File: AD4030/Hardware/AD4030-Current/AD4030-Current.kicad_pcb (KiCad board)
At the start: 2 copper layers, 0 parts

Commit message: Hardware
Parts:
- added C301: 0.1u, Capacitor_SMD:C_0603_1608Metric_Pad1.08x0.95mm_HandSolder, F.Cu at (-9.39, 62.3)
- added C302: 0.1u, Capacitor_SMD:C_0402_1005Metric_Pad0.74x0.62mm_HandSolder, B.Cu at (171.1, 102.2)
- added C303: 0.1u, Capacitor_SMD:C_0402_1005Metric_Pad0.74x0.62mm_HandSolder, B.Cu at (171.1, 103.3)
- added C304: 0.1u, Capacitor_SMD:C_0402_1005Metric_Pad0.74x0.62mm_HandSolder, B.Cu at (175.3, 93.6)
- added C305: 0.1u, Capacitor_SMD:C_0402_1005Metric_Pad0.74x0.62mm_HandSolder, B.Cu at (175.3, 94.6)
- added C306: 0.1u, Capacitor_SMD:C_0402_1005Metric_Pad0.74x0.62mm_HandSolder, B.Cu at (172.5, 93.6)
- added C307: 560p, Capacitor_SMD:C_0402_1005Metric_Pad0.74x0.62mm_HandSolder, F.Cu at (165.5, 99.0)
- added C308: 560p, Capacitor_SMD:C_0402_1005Metric_Pad0.74x0.62mm_HandSolder, F.Cu at (165.5, 94.3)
- added C309: 0.1u, Capacitor_SMD:C_0402_1005Metric_Pad0.74x0.62mm_HandSolder, B.Cu at (172.5, 94.6)
- added C310: 270p, Capacitor_SMD:C_0402_1005Metric_Pad0.74x0.62mm_HandSolder, F.Cu at (167.3, 96.6)
- added C311: 1u, Capacitor_SMD:C_0603_1608Metric_Pad1.08x0.95mm_HandSolder, B.Cu at (169.8, 90.9)
- added C312: 0.1u, Capacitor_SMD:C_0603_1608Metric_Pad1.08x0.95mm_HandSolder, F.Cu at (-9.39, 67.3)
- added C313: 0.1u, Capacitor_SMD:C_0603_1608Metric_Pad1.08x0.95mm_HandSolder, F.Cu at (-9.39, 69.8)
- added C314: 2u2/25V, Capacitor_SMD:C_0805_2012Metric_Pad1.18x1.45mm_HandSolder, B.Cu at (152.5, 82.2)
- added C315: 10u, Capacitor_SMD:C_0805_2012Metric_Pad1.18x1.45mm_HandSolder, B.Cu at (152.5, 86.4)
- added C316: 1u, Capacitor_SMD:C_0603_1608Metric_Pad1.08x0.95mm_HandSolder, F.Cu at (176.3, 90.9)
- added C317: 2n7, Capacitor_SMD:C_0603_1608Metric_Pad1.08x0.95mm_HandSolder, B.Cu at (173.9, 90.9)
- added C318: 10u, Capacitor_SMD:C_0805_2012Metric_Pad1.18x1.45mm_HandSolder, B.Cu at (152.5, 84.2)
- added C319: 10u, Capacitor_SMD:C_0805_2012Metric_Pad1.18x1.45mm_HandSolder, F.Cu at (163.2, 90.9)
- added C320: 0.1u, Capacitor_SMD:C_0603_1608Metric_Pad1.08x0.95mm_HandSolder, F.Cu at (-41.0, 49.7)
- added C321: 1u, Capacitor_SMD:C_0603_1608Metric_Pad1.08x0.95mm_HandSolder, F.Cu at (-41.0, 52.2)
- added C322: 0.1u, Capacitor_SMD:C_0603_1608Metric_Pad1.08x0.95mm_HandSolder, F.Cu at (-41.0, 54.7)
- added C323: 1u, Capacitor_SMD:C_0603_1608Metric_Pad1.08x0.95mm_HandSolder, F.Cu at (-41.0, 57.2)
- added C401: 0.1u, Capacitor_SMD:C_0603_1608Metric_Pad1.08x0.95mm_HandSolder, F.Cu at (-36.7, 49.7)
- added C402: 1u, Capacitor_SMD:C_0603_1608Metric_Pad1.08x0.95mm_HandSolder, F.Cu at (-36.7, 52.2)
- added C403: 0.1u, Capacitor_SMD:C_0603_1608Metric_Pad1.08x0.95mm_HandSolder, F.Cu at (-36.7, 54.7)
- added C404: 1u, Capacitor_SMD:C_0603_1608Metric_Pad1.08x0.95mm_HandSolder, F.Cu at (-36.7, 57.2)
- added C405: 0.1u, Capacitor_SMD:C_0603_1608Metric_Pad1.08x0.95mm_HandSolder, F.Cu at (-32.3, 49.7)
- added C406: 1u, Capacitor_SMD:C_0603_1608Metric_Pad1.08x0.95mm_HandSolder, F.Cu at (-32.3, 52.2)
- added C407: 0.1u, Capacitor_SMD:C_0603_1608Metric_Pad1.08x0.95mm_HandSolder, F.Cu at (-32.3, 54.7)
- added C408: 1u, Capacitor_SMD:C_0603_1608Metric_Pad1.08x0.95mm_HandSolder, F.Cu at (-32.3, 57.2)
- added C409: C, Capacitor_SMD:C_0603_1608Metric_Pad1.08x0.95mm_HandSolder, F.Cu at (124.3, 99.8)
- added C410: C, Capacitor_SMD:C_0603_1608Metric_Pad1.08x0.95mm_HandSolder, F.Cu at (136.0, 99.8)
- added C411: C, Capacitor_SMD:C_0603_1608Metric_Pad1.08x0.95mm_HandSolder, F.Cu at (147.7, 99.8)
- added C412: 0.1u, Capacitor_SMD:C_0603_1608Metric_Pad1.08x0.95mm_HandSolder, B.Cu at (113.0, 97.6)
- added C413: 0.1u, Capacitor_SMD:C_0603_1608Metric_Pad1.08x0.95mm_HandSolder, B.Cu at (121.1, 97.6)
- added C414: 0.1u, Capacitor_SMD:C_0603_1608Metric_Pad1.08x0.95mm_HandSolder, B.Cu at (132.8, 97.6)
- added C415: 0.1u, Capacitor_SMD:C_0603_1608Metric_Pad1.08x0.95mm_HandSolder, B.Cu at (144.5, 97.6)
- added C416: 0.1u, Capacitor_SMD:C_0603_1608Metric_Pad1.08x0.95mm_HandSolder, B.Cu at (120.8, 104.0)
- added C417: 0.1u, Capacitor_SMD:C_0603_1608Metric_Pad1.08x0.95mm_HandSolder, F.Cu at (-0.29, 38.1)
- added C418: 0.1u, Capacitor_SMD:C_0603_1608Metric_Pad1.08x0.95mm_HandSolder, F.Cu at (4.06, 18.0)
- added C419: 0.1u, Capacitor_SMD:C_0603_1608Metric_Pad1.08x0.95mm_HandSolder, B.Cu at (108.1, 97.6)
- added C420: 0.1u, Capacitor_SMD:C_0603_1608Metric_Pad1.08x0.95mm_HandSolder, B.Cu at (116.1, 97.6)
- added C421: 0.1u, Capacitor_SMD:C_0603_1608Metric_Pad1.08x0.95mm_HandSolder, B.Cu at (127.7, 97.6)
- added C422: 0.1u, Capacitor_SMD:C_0603_1608Metric_Pad1.08x0.95mm_HandSolder, B.Cu at (139.4, 97.6)
- added C423: 0.1u, Capacitor_SMD:C_0603_1608Metric_Pad1.08x0.95mm_HandSolder, B.Cu at (116.3, 104.0)
- added C424: 0.1u, Capacitor_SMD:C_0603_1608Metric_Pad1.08x0.95mm_HandSolder, F.Cu at (4.06, 33.1)
- added C425: 0.1u, Capacitor_SMD:C_0603_1608Metric_Pad1.08x0.95mm_HandSolder, F.Cu at (4.06, 35.6)
- added C426: 0.1u, Capacitor_SMD:C_0603_1608Metric_Pad1.08x0.95mm_HandSolder, F.Cu at (4.06, 38.1)
- added C427: 0.1u, Capacitor_SMD:C_0603_1608Metric_Pad1.08x0.95mm_HandSolder, F.Cu at (8.41, 18.0)
- added C428: 0.1u, Capacitor_SMD:C_0603_1608Metric_Pad1.08x0.95mm_HandSolder, F.Cu at (8.41, 20.5)
- added C429: 0.1u, Capacitor_SMD:C_0603_1608Metric_Pad1.08x0.95mm_HandSolder, F.Cu at (8.41, 23.0)
- added C430: 0.1u, Capacitor_SMD:C_0603_1608Metric_Pad1.08x0.95mm_HandSolder, F.Cu at (8.41, 25.5)
- added C431: 0.1u, Capacitor_SMD:C_0603_1608Metric_Pad1.08x0.95mm_HandSolder, F.Cu at (8.41, 28.0)
- added C432: 1n, Capacitor_SMD:C_0603_1608Metric_Pad1.08x0.95mm_HandSolder, F.Cu at (151.5, 96.6)
- added C433: 2n2, Capacitor_SMD:C_0603_1608Metric_Pad1.08x0.95mm_HandSolder, F.Cu at (154.2, 93.0)
- added C434: 0.1u, Capacitor_SMD:C_0603_1608Metric_Pad1.08x0.95mm_HandSolder, F.Cu at (8.41, 35.6)
- added C435: 0.1u, Capacitor_SMD:C_0603_1608Metric_Pad1.08x0.95mm_HandSolder, F.Cu at (8.41, 38.1)
- added C436: 0.1u, Capacitor_SMD:C_0603_1608Metric_Pad1.08x0.95mm_HandSolder, F.Cu at (12.8, 18.0)
- added C437: 0.1u, Capacitor_SMD:C_0603_1608Metric_Pad1.08x0.95mm_HandSolder, F.Cu at (12.8, 20.5)
- added C501: 2u2/35V, Capacitor_SMD:C_1206_3216Metric_Pad1.33x1.80mm_HandSolder, F.Cu at (167.9, 85.3)
- added C502: 10u/50V, Capacitor_SMD:C_1210_3225Metric_Pad1.33x2.70mm_HandSolder, B.Cu at (196.7, 69.7)
- added C503: 10u/50V, Capacitor_SMD:C_1210_3225Metric_Pad1.33x2.70mm_HandSolder, B.Cu at (187.7, 71.9)
- added C504: 2u2/35V, Capacitor_SMD:C_1206_3216Metric_Pad1.33x1.80mm_HandSolder, F.Cu at (160.5, 85.3)
- added C505: 2u2/35V, Capacitor_SMD:C_1206_3216Metric_Pad1.33x1.80mm_HandSolder, F.Cu at (160.4, 79.6)
- added C506: 10u/50V, Capacitor_SMD:C_1210_3225Metric_Pad1.33x2.70mm_HandSolder, B.Cu at (192.7, 69.7)
- added C507: 10u/50V, Capacitor_SMD:C_1210_3225Metric_Pad1.33x2.70mm_HandSolder, B.Cu at (183.6, 71.9)
- added C508: 2u2/35V, Capacitor_SMD:C_1206_3216Metric_Pad1.33x1.80mm_HandSolder, F.Cu at (167.9, 79.6)
- added C509: 10u/25V, Capacitor_SMD:C_1206_3216Metric_Pad1.33x1.80mm_HandSolder, F.Cu at (160.7, 66.8)
- added C510: 10u/25V, Capacitor_SMD:C_1206_3216Metric_Pad1.33x1.80mm_HandSolder, F.Cu at (190.6, 77.0)
- added C511: 10u/25V, Capacitor_SMD:C_1206_3216Metric_Pad1.33x1.80mm_HandSolder, F.Cu at (152.9, 66.8)
- added C512: 2u2/35V, Capacitor_SMD:C_1206_3216Metric_Pad1.33x1.80mm_HandSolder, F.Cu at (33.6, 64.5)
- added C513: 0.01u, Capacitor_SMD:C_0603_1608Metric_Pad1.08x0.95mm_HandSolder, F.Cu at (198.1, 76.1)
- added C514: 2u2/35V, Capacitor_SMD:C_1206_3216Metric_Pad1.33x1.80mm_HandSolder, F.Cu at (33.6, 67.8)
- added C515: 2u2, Capacitor_SMD:C_0805_2012Metric_Pad1.18x1.45mm_HandSolder, B.Cu at (191.5, 80.8)
- added C516: 2u2/35V, Capacitor_SMD:C_1206_3216Metric_Pad1.33x1.80mm_HandSolder, F.Cu at (39.6, 57.8)
- added C517: 1u, Capacitor_SMD:C_0805_2012Metric_Pad1.18x1.45mm_HandSolder, F.Cu at (191.5, 80.8)
- added C518: 2u2/35V, Capacitor_SMD:C_1206_3216Metric_Pad1.33x1.80mm_HandSolder, F.Cu at (39.6, 61.1)
- added C519: 10u/25V, Capacitor_SMD:C_1206_3216Metric_Pad1.33x1.80mm_HandSolder, F.Cu at (160.5, 73.9)
- added C520: 10u/25V, Capacitor_SMD:C_1206_3216Metric_Pad1.33x1.80mm_HandSolder, F.Cu at (167.8, 73.9)
- added D501: BZX84C10LT1G, Package_TO_SOT_SMD:SOT-23, F.Cu at (207.0, 79.9)
- added D502: 1N4148W, Diode_SMD:D_SOD-123, B.Cu at (201.9, 72.1)
- added F501: 1812L075/33DR, Fuse:Fuse_1812_4532Metric_Pad1.30x3.40mm_HandSolder, B.Cu at (207.0, 70.5)
- added FB301: FBMJ2125HM330-T, Inductor_SMD:L_0805_2012Metric_Pad1.15x1.40mm_HandSolder, F.Cu at (-9.19, 82.2)
- added J401: Conn_01x08, Connector_PinHeader_2.54mm:PinHeader_1x08_P2.54mm_Vertical_SMD_Pin1Right, B.Cu at (196.2, 94.4)
- added J402: Conn_01x07, Connector_PinHeader_2.54mm:PinHeader_1x07_P2.54mm_Vertical_SMD_Pin1Right, B.Cu at (196.3, 114.6)
- added J403: PMOD, Connector_PinHeader_2.54mm:PinHeader_2x06_P2.54mm_Horizontal, F.Cu at (203.2, 86.5)
- added J404: PMOD, Connector_PinHeader_2.54mm:PinHeader_2x06_P2.54mm_Horizontal, F.Cu at (203.3, 104.9)
- added J501: 1715721, TerminalBlock_Phoenix:TerminalBlock_Phoenix_MKDS-1,5-2_1x02_P5.00mm_Horizontal, F.Cu at (207.0, 65.1)
- added L503: TCK-141, Inductor_SMD:L_TracoPower_TCK-141, F.Cu at (194.6, 71.5)
- added L504: TCK-133, AD4030:TCK-133, F.Cu at (185.7, 73.0)
- added Q501: SI5618A, Package_TO_SOT_SMD:SOT-23, F.Cu at (207.0, 74.8)
- added Q502: MMBT3904, Package_TO_SOT_SMD:SOT-23, F.Cu at (201.9, 74.8)
- added R301: 0, Resistor_SMD:R_0603_1608Metric_Pad0.98x0.95mm_HandSolder, F.Cu at (171.6, 82.4)
- added R302: 33, Resistor_SMD:R_0603_1608Metric_Pad0.98x0.95mm_HandSolder, F.Cu at (175.9, 87.2)
- added R305: 33, Resistor_SMD:R_0402_1005Metric_Pad0.72x0.64mm_HandSolder, F.Cu at (165.5, 97.1)
- added R306: 33, Resistor_SMD:R_0402_1005Metric_Pad0.72x0.64mm_HandSolder, F.Cu at (165.5, 96.1)
- added R307: 100, Resistor_SMD:R_0603_1608Metric_Pad0.98x0.95mm_HandSolder, F.Cu at (169.8, 90.9)
- added R308: OPT, Resistor_SMD:R_0603_1608Metric_Pad0.98x0.95mm_HandSolder, F.Cu at (171.4, 90.9)
- added R309: 10k, Resistor_SMD:R_0603_1608Metric_Pad0.98x0.95mm_HandSolder, F.Cu at (173.9, 90.9)
- added R401: 51, Resistor_SMD:R_0402_1005Metric_Pad0.72x0.64mm_HandSolder, F.Cu at (200.2, 95.2)
- added R402: 51, Resistor_SMD:R_0402_1005Metric_Pad0.72x0.64mm_HandSolder, F.Cu at (200.2, 92.8)
- added R403: 51, Resistor_SMD:R_0402_1005Metric_Pad0.72x0.64mm_HandSolder, F.Cu at (200.2, 90.2)
- added R404: 51, Resistor_SMD:R_0402_1005Metric_Pad0.72x0.64mm_HandSolder, F.Cu at (200.3, 113.7)
- added R405: 51, Resistor_SMD:R_0402_1005Metric_Pad0.72x0.64mm_HandSolder, F.Cu at (200.3, 111.3)
- added R406: 51, Resistor_SMD:R_0402_1005Metric_Pad0.72x0.64mm_HandSolder, F.Cu at (200.3, 108.6)
- added R407: 51, Resistor_SMD:R_0402_1005Metric_Pad0.72x0.64mm_HandSolder, F.Cu at (200.2, 96.6)
- added R408: 51, Resistor_SMD:R_0402_1005Metric_Pad0.72x0.64mm_HandSolder, F.Cu at (200.2, 94.0)
- added R409: 51, Resistor_SMD:R_0402_1005Metric_Pad0.72x0.64mm_HandSolder, F.Cu at (200.2, 91.6)
- added R410: 51, Resistor_SMD:R_0402_1005Metric_Pad0.72x0.64mm_HandSolder, F.Cu at (200.3, 115.1)
- added R411: 51, Resistor_SMD:R_0402_1005Metric_Pad0.72x0.64mm_HandSolder, F.Cu at (200.3, 112.5)
- added R412: 51, Resistor_SMD:R_0402_1005Metric_Pad0.72x0.64mm_HandSolder, F.Cu at (200.3, 110.0)
- added R413: WSBS85181L000JK35, AD4030:WSBS8518-35, F.Cu at (94.5, 95.0)
- added R414: 0, Resistor_SMD:R_0603_1608Metric_Pad0.98x0.95mm_HandSolder, F.Cu at (110.6, 102.6)
- added R415: 2k49, Resistor_SMD:R_0603_1608Metric_Pad0.98x0.95mm_HandSolder, F.Cu at (155.8, 99.4)
- added R416: 1k58, Resistor_SMD:R_0603_1608Metric_Pad0.98x0.95mm_HandSolder, F.Cu at (157.6, 93.0)
- added R501: 100k, Resistor_SMD:R_0603_1608Metric_Pad0.98x0.95mm_HandSolder, F.Cu at (202.1, 79.9)
- added R502: 100k, Resistor_SMD:R_0603_1608Metric_Pad0.98x0.95mm_HandSolder, B.Cu at (201.9, 69.2)
- added R503: 10k5, Resistor_SMD:R_0603_1608Metric_Pad0.98x0.95mm_HandSolder, F.Cu at (195.5, 80.8)
- added R504: 10k, Resistor_SMD:R_0603_1608Metric_Pad0.98x0.95mm_HandSolder, F.Cu at (198.1, 79.9)
- added R505: R, Resistor_SMD:R_0603_1608Metric_Pad0.98x0.95mm_HandSolder, F.Cu at (159.9, 62.8)
- added R506: 0, Resistor_SMD:R_0603_1608Metric_Pad0.98x0.95mm_HandSolder, B.Cu at (190.6, 77.0)
- added R507: R, Resistor_SMD:R_0603_1608Metric_Pad0.98x0.95mm_HandSolder, F.Cu at (156.5, 62.8)
- added R508: R, Resistor_SMD:R_0603_1608Metric_Pad0.98x0.95mm_HandSolder, F.Cu at (22.4, 62.4)
- added R509: R, Resistor_SMD:R_0603_1608Metric_Pad0.98x0.95mm_HandSolder, F.Cu at (22.4, 64.9)
- added R510: R, Resistor_SMD:R_0603_1608Metric_Pad0.98x0.95mm_HandSolder, F.Cu at (22.4, 67.4)
- added R511: R, Resistor_SMD:R_0603_1608Metric_Pad0.98x0.95mm_HandSolder, F.Cu at (22.4, 69.9)
- added RN301: MPMT2003AT5, Package_TO_SOT_SMD:SOT-23, F.Cu at (166.0, 90.9)
- added RN401: MPMT10019001AT1, Package_TO_SOT_SMD:SOT-23, F.Cu at (124.3, 96.6)
- added RN402: MPMT10019001AT1, Package_TO_SOT_SMD:SOT-23, F.Cu at (136.0, 96.6)
- added RN403: MPMT10019001AT1, Package_TO_SOT_SMD:SOT-23, F.Cu at (147.7, 96.6)
- added RV401: 3224W-1-103E, Potentiometer_SMD:Potentiometer_Bourns_3224W_Vertical, F.Cu at (118.6, 91.0)
- added RV402: 3224W-1-103E, Potentiometer_SMD:Potentiometer_Bourns_3224W_Vertical, F.Cu at (130.3, 91.0)
- added RV403: 3224W-1-103E, Potentiometer_SMD:Potentiometer_Bourns_3224W_Vertical, F.Cu at (142.0, 91.0)
- added U301: AD8475ACPZ, Package_CSP:LFCSP-16-1EP_3x3mm_P0.5mm_EP1.6x1.6mm, F.Cu at (161.8, 96.6)
- added U302: SN74AUC1G79DBVR, Package_TO_SOT_SMD:SOT-23-5_HandSoldering, F.Cu at (175.9, 83.4)
- added U303: AD4030-24, AD4030:05-08-1797_ADI, F.Cu at (173.1, 97.8)
- added U304: LTC6655BHMS8-5, Package_SO:MSOP-8_3x3mm_P0.65mm, F.Cu at (152.5, 84.2)
- added U305: ADuM260N, Package_SO:SOIC-16W_7.5x12.8mm_P1.27mm, B.Cu at (185.9, 107.1)
- added U401: ADuM260N, Package_SO:SOIC-16W_7.5x12.8mm_P1.27mm, F.Cu at (185.9, 93.7)
- added U402: ADuM260N, Package_SO:SOIC-16W_7.5x12.8mm_P1.27mm, F.Cu at (185.9, 107.1)
- added U403: AD8479, Package_SO:SOIC-8_3.9x4.9mm_P1.27mm, F.Cu at (110.6, 97.6)
- added U404: ADG5236BCPZ, Package_DFN_QFN:QFN-16-1EP_4x4mm_P0.65mm_EP2.5x2.5mm_ThermalVias, F.Cu at (118.6, 104.0)
- added U405: ADG5236BCPZ, Package_DFN_QFN:QFN-16-1EP_4x4mm_P0.65mm_EP2.5x2.5mm_ThermalVias, F.Cu at (130.3, 104.0)
- added U406: ADG5236BCPZ, Package_DFN_QFN:QFN-16-1EP_4x4mm_P0.65mm_EP2.5x2.5mm_ThermalVias, F.Cu at (142.0, 104.0)
- added U407: AD797ARZ, Package_SO:SOIC-8_3.9x4.9mm_P1.27mm, F.Cu at (118.6, 97.6)
- added U408: AD797ARZ, Package_SO:SOIC-8_3.9x4.9mm_P1.27mm, F.Cu at (130.3, 97.6)
- added U409: AD797ARZ, Package_SO:SOIC-8_3.9x4.9mm_P1.27mm, F.Cu at (142.0, 97.6)
- added U410: TXB0101DBV, Package_TO_SOT_SMD:SOT-23-6, F.Cu at (124.3, 104.0)
- added U411: TXB0101DBV, Package_TO_SOT_SMD:SOT-23-6, F.Cu at (136.0, 104.0)
- added U412: TXB0101DBV, Package_TO_SOT_SMD:SOT-23-6, F.Cu at (147.7, 104.0)
- added U413: ADA4077-1xRM, Package_SO:MSOP-8_3x3mm_P0.65mm, F.Cu at (155.8, 96.6)
- added U414: ADG5236BCPZ, Package_DFN_QFN:QFN-16-1EP_4x4mm_P0.65mm_EP2.5x2.5mm_ThermalVias, F.Cu at (153.1, 104.0)
- added U415: TXB0101DBV, Package_TO_SOT_SMD:SOT-23-6, F.Cu at (158.7, 104.0)
- added U501: ADP7142AUJZ-1.8, Package_TO_SOT_SMD:TSOT-23-5, F.Cu at (164.1, 79.6)
- added U502: TSR_1-2433, Converter_DCDC:Converter_DCDC_TRACO_TSR-1_THT, F.Cu at (195.1, 62.6)
- added U503: TEC3-2419WI, Converter_DCDC:Converter_DCDC_TRACO_TMR-xxxx_THT, F.Cu at (183.8, 66.6)
- added U504: LT1763CDE-ADJ, Package_DFN_QFN:DFN-12-1EP_3x4mm_P0.5mm_EP1.7x3.3mm, F.Cu at (194.7, 77.0)
- added U505: LM1117LD-3.3, Package_SON:WSON-8-1EP_4x4mm_P0.8mm_EP2.2x3mm, F.Cu at (164.2, 73.9)
- added U506: ADP5070AREZ, Package_SO:ETSSOP-20-1EP_4.4x6.5mm_P0.65mm_EP3x4.2mm, F.Cu at (145.4, 65.8)
- added U507: ADP7182AUJZ, Package_TO_SOT_SMD:TSOT-23-5, F.Cu at (152.9, 73.5)
- added U508: ADP7142AUJZ, Package_TO_SOT_SMD:TSOT-23-5, F.Cu at (144.2, 73.5)
- added U509: LM1117LD-ADJ, Package_SON:WSON-8-1EP_4x4mm_P0.8mm_EP2.2x3mm, F.Cu at (157.1, 66.8)
- added U510: ADP7142AUJZ-1.8, Package_TO_SOT_SMD:TSOT-23-5, F.Cu at (164.2, 85.3)
- added X301: ECS-2520MV-1000-BN-TR, Oscillator:Oscillator_SMD_ECS_2520MV-xxx-xx-4Pin_2.5x2.0mm, F.Cu at (171.6, 85.9)
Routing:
- net unconnected-(U503-NC-Pad5): track 0.00 -> 28.1 mm
- added copper zone on B.Cu, net GNDS
- added copper zone on F.Cu, net GNDS
- added copper zone on In1.Cu, net GNDS
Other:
- board outline added: 125 x 70 mm
- copper layers 2 -> 4

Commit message: Hardware
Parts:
- added C521: 1u, Capacitor_SMD:C_0603_1608Metric_Pad1.08x0.95mm_HandSolder, B.Cu at (141.4, 82.7)
- added C522: 0.1u, Capacitor_SMD:C_0603_1608Metric_Pad1.08x0.95mm_HandSolder, B.Cu at (130.3, 82.7)
- added C523: 68n, Capacitor_SMD:C_0603_1608Metric_Pad1.08x0.95mm_HandSolder, F.Cu at (150.0, 67.6)
- added C524: 47n, Capacitor_SMD:C_0603_1608Metric_Pad1.08x0.95mm_HandSolder, F.Cu at (150.0, 71.2)
- added C525: 1u, Capacitor_SMD:C_0603_1608Metric_Pad1.08x0.95mm_HandSolder, F.Cu at (145.0, 63.9)
- added C526: 10u/35V, Capacitor_SMD:C_1206_3216Metric_Pad1.33x1.80mm_HandSolder, F.Cu at (128.9, 72.0)
- added C527: 10u/35V, Capacitor_SMD:C_1206_3216Metric_Pad1.33x1.80mm_HandSolder, F.Cu at (128.9, 65.5)
- added C528: 1u, Capacitor_SMD:C_0603_1608Metric_Pad1.08x0.95mm_HandSolder, B.Cu at (147.4, 63.9)
- added C529: 10u/35V, Capacitor_SMD:C_1206_3216Metric_Pad1.33x1.80mm_HandSolder, F.Cu at (140.3, 63.4)
- added D503: DFLS240-7, AD4030:POWERDI123_DIO, F.Cu at (134.0, 73.7)
- added D504: DFLS240-7, AD4030:POWERDI123_DIO, F.Cu at (134.0, 64.0)
- added L501: XAL4030-682MEC, Inductor_SMD:L_Coilcraft_XAL4030-XXX, F.Cu at (139.6, 73.7)
- added L502: XAL4040-153MEB, Inductor_SMD:L_Coilcraft_XAL4040-XXX, F.Cu at (133.9, 69.1)
- added R512: 1k, Resistor_SMD:R_0603_1608Metric_Pad0.98x0.95mm_HandSolder, B.Cu at (141.4, 80.9)
- added R513: 4k64, Resistor_SMD:R_0603_1608Metric_Pad0.98x0.95mm_HandSolder, B.Cu at (130.3, 80.9)
- added R514: 15k, Resistor_SMD:R_0603_1608Metric_Pad0.98x0.95mm_HandSolder, F.Cu at (147.4, 67.6)
- added R515: 12k, Resistor_SMD:R_0603_1608Metric_Pad0.98x0.95mm_HandSolder, F.Cu at (147.4, 71.2)
- added R516: 2M15, Resistor_SMD:R_0603_1608Metric_Pad0.98x0.95mm_HandSolder, F.Cu at (147.4, 74.9)
- added R517: 113k, Resistor_SMD:R_0603_1608Metric_Pad0.98x0.95mm_HandSolder, F.Cu at (145.0, 74.9)
- added R518: 100k, Resistor_SMD:R_0603_1608Metric_Pad0.98x0.95mm_HandSolder, F.Cu at (147.4, 63.9)
- added R519: 2M1, Resistor_SMD:R_0603_1608Metric_Pad0.98x0.95mm_HandSolder, F.Cu at (149.9, 63.9)
- added R520: 10k, Resistor_SMD:R_0603_1608Metric_Pad0.98x0.95mm_HandSolder, F.Cu at (145.0, 71.2)
- added R521: 10k, Resistor_SMD:R_0603_1608Metric_Pad0.98x0.95mm_HandSolder, F.Cu at (145.0, 67.6)
- C312, C313, C320, C321, C401, C402, C403, C404, C405, C406, C407, C408, C417, C418, C424, C425, C426, C427, C428, C429, C430, C431, C434, C435, C436, C437: moved to B.Cu
- R505: value R -> 3k32
- R507: value R -> 1k
- R508: value R -> 20k
- R509: value R -> 10k
- R510: value R -> 52k3
- R511: value R -> 4k64
- U403: value AD8479 -> AD8479ARZ
- U506: value ADP5070AREZ -> ADP5070ACPZ; footprint Package_SO:ETSSOP-20-1EP_4.4x6.5mm_P0.65mm_EP3x4.2mm -> Package_DFN_QFN:QFN-20-1EP_4x4mm_P0.5mm_EP2.6x2.6mm_ThermalVias
- moved C323 240.2 mm to (192.0, 115.4), turned to -90 degrees
- moved C322 239.4 mm to (190.5, 115.4), turned to -90 degrees
- moved C408 228.1 mm to (192.0, 98.7), turned to 90 degrees
- moved C321 227.3 mm to (178.2, 112.5), turned to -90 degrees
- moved C407 227.1 mm to (190.5, 98.7), turned to 90 degrees
- moved C405 226.6 mm to (190.5, 91.1), turned to -90 degrees
- moved C320 225.7 mm to (175.8, 112.5), turned to -90 degrees
- moved C406 225.6 mm to (190.5, 87.4), turned to 90 degrees
- moved C402 220.9 mm to (178.2, 103.6), turned to -90 degrees
- moved C401 219.3 mm to (175.9, 103.6), turned to -90 degrees
- moved C404 217.5 mm to (178.3, 90.0), turned to -90 degrees
- moved C403 215.6 mm to (176.1, 90.0), turned to -90 degrees
- moved C312 184.7 mm to (174.6, 83.4), turned to 90 degrees
- moved C313 181.6 mm to (171.6, 85.1), turned to 180 degrees
- moved C301 175.4 mm to (161.8, 100.5)
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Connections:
- C301 pad 1: +5VA -> +5V4
- U301 pad 6: +5VA -> +5V4
- U301 pad 7: +5VA -> +5V4
- U301 pad 8: +5VA -> +5V4
- U506 pad 1: unconnected-(U506-PGND-Pad1) -> Net-(U506-INBK)
- U506 pad 10: unconnected-(U506-SS-Pad10) -> Net-(U506-COMP2)
- U506 pad 11: unconnected-(U506-EN2-Pad11) -> Net-(U506-FB2)
- U506 pad 12: unconnected-(U506-COMP2-Pad12) -> Net-(U506-VREF)
- U506 pad 13: unconnected-(U506-FB2-Pad13) -> GND
- U506 pad 14: unconnected-(U506-VREF-Pad14) -> Net-(U506-VREG)
- U506 pad 15: Net-(U506-AGND) -> +9V
- U506 pad 16: unconnected-(U506-VREG-Pad16) -> +9V
- U506 pad 17: unconnected-(U506-PVIN1-Pad17) -> +9V
- U506 pad 18: unconnected-(U506-PVINSYS-Pad18) -> Net-(D504-K)
- U506 pad 19: unconnected-(U506-PVIN2-Pad19) -> GND
- U506 pad 2: unconnected-(U506-SW1-Pad2) -> GND
- U506 pad 20: unconnected-(U506-SW2-Pad20) -> Net-(D503-A)
- U506 pad 21: Net-(U506-AGND) -> GND
- U506 pad 5: unconnected-(U506-SEQ-Pad5) -> Net-(U506-FB1)
- U506 pad 6: unconnected-(U506-SLEW-Pad6) -> Net-(U506-COMP1)
- U506 pad 7: unconnected-(U506-FB1-Pad7) -> Net-(U506-EN1)
- U506 pad 9: unconnected-(U506-EN1-Pad9) -> Net-(U506-EN1)
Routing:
- net GND: vias 0 -> 5
- net +5V4: vias 0 -> 7
- net +3.3V: vias 0 -> 10

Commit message: PCB layout
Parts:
- added C430: 0.1u, Capacitor_SMD:C_0603_1608Metric_Pad1.08x0.95mm_HandSolder, B.Cu at (158.2, 96.6)
- added C431: 0.1u, Capacitor_SMD:C_0603_1608Metric_Pad1.08x0.95mm_HandSolder, B.Cu at (153.4, 96.6)
- added R304: 51, Resistor_SMD:R_0402_1005Metric_Pad0.72x0.64mm_HandSolder, F.Cu at (200.3, 116.3)
- added R311: 51, Resistor_SMD:R_0402_1005Metric_Pad0.72x0.64mm_HandSolder, F.Cu at (200.3, 117.6)
- moved C521 10.9 mm to (129.7, 85.6)
- moved C520 10.4 mm to (140.7, 85.6)
- moved C428 7.22 mm to (151.1, 99.6)
- moved R404 6.62 mm to (158.0, 99.6)
- moved R403 1.28 mm to (154.6, 99.6)
- moved D504 1.02 mm to (133.0, 64.0)
- moved R516 0.93 mm to (158.3, 68.3)
- moved R521 0.93 mm to (154.8, 68.3)
- moved D503 0.90 mm to (133.1, 73.5)
- moved L501 0.65 mm to (138.9, 73.5)
- moved L502 0.41 mm to (133.5, 69.0)
- moved C523 0.25 mm to (160.1, 85.0)
- moved C525 0.25 mm to (160.1, 73.5)
- moved C424 0.25 mm to (136.0, 102.9)
- moved C425 0.25 mm to (147.7, 102.9)
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- renumbered C301 to C201, C302 to C202, C303 to C203, C304 to C204, C305 to C205, C306 to C206, C309 to C207, C307 to C208, C308 to C209, C310 to C210, C311 to C211, C312 to C212, C313 to C213, C314 to C214, C315 to C215, C316 to C216, C317 to C217, C318 to C218, C319 to C219, C401 to C301, C320 to C302, C402 to C303, C321 to C304, C403 to C305, C404 to C306, C405 to C307, C322 to C308, C406 to C309, C323 to C310, C407 to C311, C408 to C312, C426 to C401, C419 to C402, C427 to C403, C420 to C404, C428 to C405, C421 to C406, C437 to C407, C422 to C408, C423 to C409, C424 to C410, C425 to C411, C434 to C412, C412 to C413, C409 to C414, C413 to C415, C414 to C416, C415 to C417, C416 to C418, C417 to C419, C410 to C420, C418 to C421, C435 to C422, C429 to C423, C430 to C424, C431 to C425, C411 to C426, C436 to C427, C433 to C428, C432 to C429, C529 to C501, C524 to C502, C523 to C503, C525 to C504, C503 to C505, C502 to C506, C528 to C507, C507 to C508, C526 to C509, C527 to C510, C506 to C511, C518 to C512, C516 to C513, C510 to C514, C511 to C515, C521 to C516, C522 to C517, C513 to C518, C509 to C519, C512 to C520, C514 to C521, C515 to C522, C504 to C523, C505 to C524, C519 to C525, C517 to C526, C520 to C527, C501 to C528, C508 to C529, FB301 to FB201, J401 to J301, J402 to J302, J403 to J303, J404 to J304, L504 to L503, L503 to L504, R301 to R201, R302 to R202, R305 to R203, R306 to R204, R307 to R205, R308 to R206, R309 to R207, R401 to R301, R402 to R302, R403 to R303, R404 to R305, R405 to R306, R406 to R307, R407 to R308, R408 to R309, R409 to R310, R410 to R312, R411 to R313, R412 to R314, R413 to R401, R414 to R402, R415 to R403, R416 to R404, R520 to R501, R521 to R502, R515 to R503, R514 to R504, R501 to R505, R502 to R506, R517 to R507, R518 to R508, R516 to R509, R519 to R510, R506 to R511, R508 to R512, R509 to R513, R511 to R514, R510 to R515, R507 to R516, R512 to R517, R503 to R518, R504 to R519, R513 to R520, R505 to R521, RN301 to RN201, U301 to U201, U302 to U202, U303 to U203, U304 to U204, U401 to U301, U402 to U302, U305 to U303, U403 to U401, U404 to U402, U407 to U403, U410 to U404, U408 to U406, U411 to U407, U406 to U408, U412 to U410, U414 to U411, U415 to U412, U506 to U501, U503 to U502, U502 to U503, U508 to U504, U507 to U505, U504 to U506, U509 to U507, U505 to U508, U510 to U509, U501 to U510, X301 to X201
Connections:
- net /Isolation/GAIN_x10B renamed /Isolation/Gain_x10B
- C401 pad 1: +5V -> +5V4
- C403 pad 1: +5V -> +5V4
- C405 pad 1: +5V -> +5V4
- C407 pad 1: +5V -> +5V4
- J302 pad 3: /Isolation/CONN_GAIN_x20 -> /Isolation/CONN_GAIN_x10A
- J302 pad 4: /Isolation/CONN_GAIN_x10 -> /Isolation/CONN_GAIN_x10B
- J302 pad 5: unconnected-(J402-Pin_5-Pad5) -> /Isolation/CONN_GAIN_x10C
- J302 pad 6: unconnected-(J402-Pin_6-Pad6) -> /Isolation/CONN_LP_FILTER
- J304 pad 11: unconnected-(J404-Pin_11-Pad11) -> Net-(J304-Pin_11)
- J304 pad 12: unconnected-(J404-Pin_12-Pad12) -> Net-(J304-Pin_12)
- U303 pad 14: unconnected-(U305-VOB-Pad14) -> /Isolation/LP_Filter
- U303 pad 15: unconnected-(U305-VOA-Pad15) -> /Isolation/Gain_x10C
- U303 pad 2: unconnected-(U305-VIA-Pad2) -> /Isolation/CONN_GAIN_x10C
- U303 pad 3: unconnected-(U305-VIB-Pad3) -> /Isolation/CONN_LP_FILTER
- U402 pad 12: +5V -> +5V4
- U404 pad 6: +5V -> +5V4
- U405 pad 12: +5V -> +5V4
- U407 pad 6: +5V -> +5V4
- U408 pad 12: +5V -> +5V4
- U410 pad 3: /Shunt/Gain_x10C -> /Isolation/Gain_x10C
- U410 pad 6: +5V -> +5V4
- U411 pad 12: +5V -> +5V4
- U412 pad 3: /Shunt/LP_FILTER -> /Isolation/LP_Filter
- U412 pad 6: +5V -> +5V4
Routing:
- net +15V: track 0.00 -> 150.0 mm, vias 0 -> 10
- net -15V: track 0.00 -> 127.4 mm, vias 0 -> 12
- net +5V4: track 0.00 -> 84.1 mm, vias 7 -> 16
- net GND: track 0.00 -> 61.0 mm, vias 5 -> 29
- net /Isolation/Gain_x10A: track 0.00 -> 51.4 mm, vias 0 -> 1
- net /Isolation/Gain_x10B: track 0.00 -> 38.4 mm
- net unconnected-(U502-NC-Pad5): track 28.1 -> 0.00 mm
- net VDDF: track 0.00 -> 26.9 mm, vias 0 -> 2
- net /Isolation/Gain_x10C: track 0.00 -> 26.4 mm
- net /Shunt/Gx10A: track 0.00 -> 22.8 mm, vias 0 -> 2
- net /Shunt/Gx10B: track 0.00 -> 22.1 mm, vias 0 -> 2
- net Net-(U413--): track 0.00 -> 21.3 mm
- net Net-(U402-Pad9): track 0.00 -> 21.1 mm
- net /Shunt/Gx10C: track 0.00 -> 20.9 mm, vias 0 -> 2
- net Net-(U405-Pad9): track 0.00 -> 20.8 mm
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- added copper zone on In2.Cu, net -15V
- added copper zone on B.Cu, net GND
- added copper zone on F.Cu, net GND
- added copper zone on In1.Cu, net GND

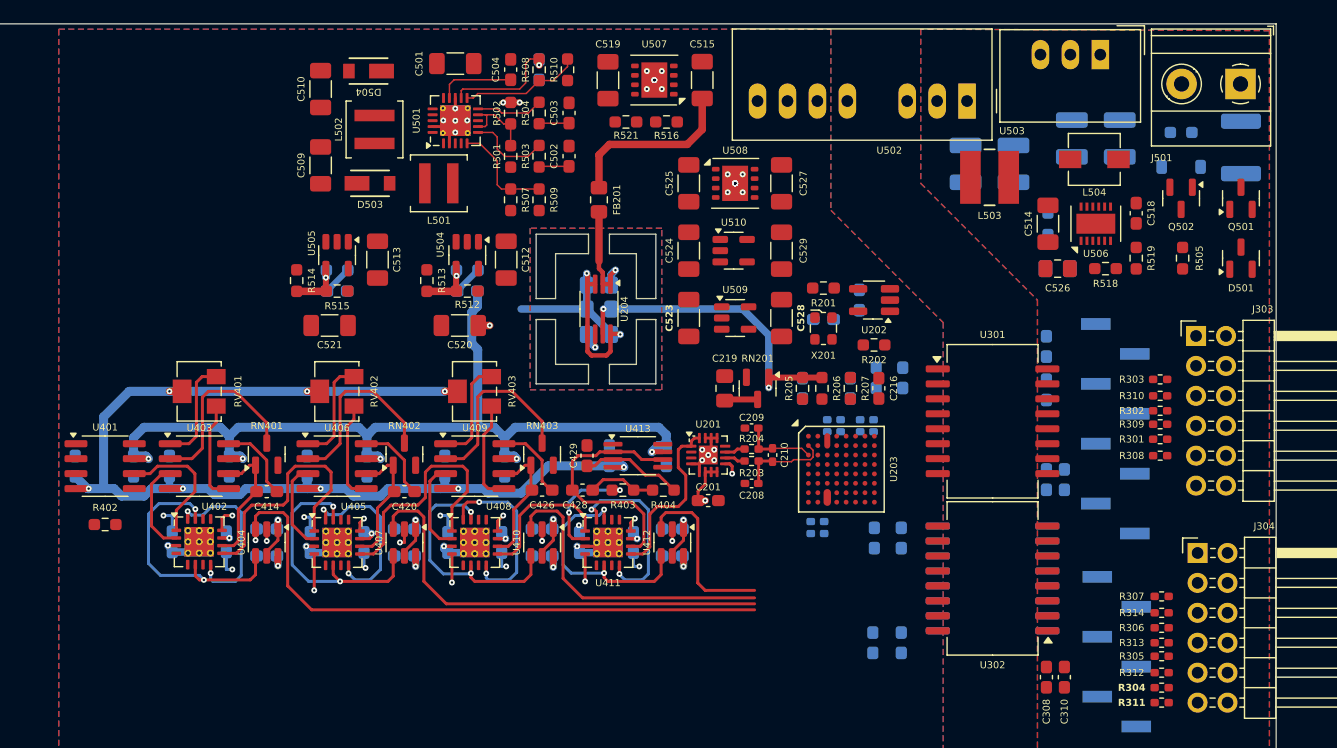
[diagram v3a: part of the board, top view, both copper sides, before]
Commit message: PCB layout for the current card
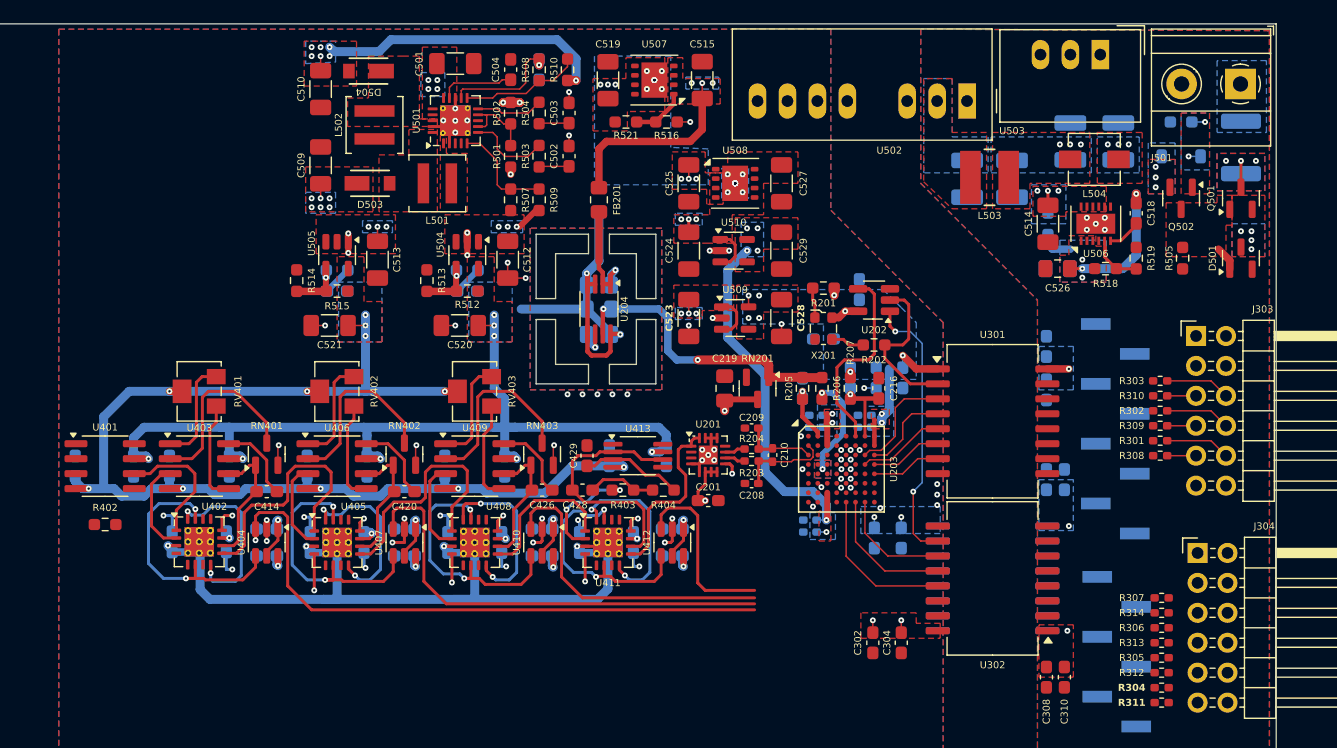
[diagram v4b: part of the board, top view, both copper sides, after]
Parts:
- C302, C304: moved to F.Cu
- moved C506 4.20 mm to (192.5, 70.0)
- moved C511 3.95 mm to (196.6, 70.0)
- moved C207 2.07 mm to (170.9, 93.2), turned to 180 degrees
- moved C206 1.65 mm to (170.9, 94.2), turned to 180 degrees
- moved C213 1.65 mm to (171.6, 86.7)
- moved C508 1.28 mm to (183.8, 73.2), turned to -90 degrees
- moved C505 1.28 mm to (187.6, 73.2), turned to -90 degrees
- moved R506 0.89 mm to (201.9, 68.3)
- moved C212 0.89 mm to (174.6, 82.5)
- moved C217 0.89 mm to (173.9, 90.0)
- moved D502 0.89 mm to (201.9, 71.2)
- moved C203 0.65 mm to (170.4, 103.1)
- moved C202 0.65 mm to (170.4, 102.1)
- moved C204 0.42 mm to (175.1, 93.2)
- moved C205 0.42 mm to (175.1, 94.2)
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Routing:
- net VIO: track 17.1 -> 99.9 mm, vias 4 -> 18
- net -15V: track 127.4 -> 204.4 mm, vias 12 -> 15
- net +15V: track 150.0 -> 189.1 mm, vias 10 -> 12
- net GND: track 61.0 -> 95.9 mm, vias 29 -> 77
- net +1V8: track 0.80 -> 32.4 mm, vias 0 -> 6
- net -16V: track 0.00 -> 27.2 mm, vias 0 -> 10
- net /ADC/ADC_CNV: track 0.00 -> 23.4 mm, vias 0 -> 2
- net +5V4: track 84.1 -> 105.4 mm, vias 16 -> 24
- net VCCQ: track 0.00 -> 16.9 mm, vias 0 -> 7
- net /ADC/SYNC_CNV: track 0.00 -> 16.8 mm
- net /ADC/CLK_100MHz: track 0.00 -> 13.4 mm
- net /ADC/ADC_~{CS}: track 0.00 -> 13.4 mm
- net VCOM: track 4.15 -> 16.1 mm, vias 1 -> 2
- net /ADC/ADC_SDI: track 0.00 -> 11.4 mm
- net +3.3V: track 0.00 -> 10.1 mm, vias 10 -> 16
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- added copper zone on B.Cu, net +15V
- added copper zone on F.Cu, net +15V
- added copper zone on B.Cu, net +16V
- added copper zone on F.Cu, net +16V
- added copper zone on In2.Cu, net +16V
- added copper zone on B.Cu, net +1V8
- added copper zone on F.Cu, net +1V8
- added copper zone on In2.Cu, net +1V8
- added copper zone on B.Cu, net +3.3V
- added copper zone on F.Cu, net +3.3V
- added copper zone on In2.Cu, net +3.3V
- added copper zone on B.Cu, net +5V4
- added copper zone on F.Cu, net +5V4
- added copper zone on In2.Cu, net +5V4
- added copper zone on B.Cu, net +9V
- added copper zone on F.Cu, net +9V
- added copper zone on In2.Cu, net +9V
- added copper zone on B.Cu, net -15V
- added copper zone on F.Cu, net -15V
- added copper zone on B.Cu, net -16V
- added copper zone on F.Cu, net -16V
- added copper zone on In2.Cu, net -16V
- added copper zone on F.Cu, net Net-(D501-A)
- added copper zone on B.Cu, net Net-(D501-K)
- added copper zone on F.Cu, net Net-(D501-K)
- added copper zone on In2.Cu, net Net-(D501-K)
- added copper zone on B.Cu, net Net-(D502-K)
- added copper zone on F.Cu, net Net-(D502-K)
- added copper zone on F.Cu, net Net-(D503-A)
- added copper zone on F.Cu, net Net-(D504-K)
- added copper zone on B.Cu, net Net-(J501-Pin_1)
- added copper zone on B.Cu, net Net-(Q501-D)
- added copper zone on F.Cu, net Net-(Q501-D)
- added copper zone on B.Cu, net Net-(R206-Pad2)
- added copper zone on F.Cu, net Net-(R206-Pad2)
- added copper zone on F.Cu, net Net-(U501-INBK)
- added copper zone on B.Cu, net Net-(U502-+VIN)
- added copper zone on F.Cu, net Net-(U502-+VIN)
- added copper zone on B.Cu, net Net-(U503-Vin)
- added copper zone on F.Cu, net Net-(U503-Vin)
- added copper zone on In2.Cu, net Net-(U503-Vin)
- added copper zone on B.Cu, net Net-(U503-Vout)
- added copper zone on F.Cu, net Net-(U503-Vout)
- added copper zone on In2.Cu, net Net-(U503-Vout)
- added copper zone on B.Cu, net VCCQ
- added copper zone on F.Cu, net VCCQ
- added copper zone on In2.Cu, net VCCQ
- added copper zone on B.Cu, net VIO
- added copper zone on F.Cu, net VIO
- added copper zone on In2.Cu, net VIO
